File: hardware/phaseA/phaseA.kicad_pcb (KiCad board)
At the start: 2 copper layers, 160 x 50 mm, 39 parts, among them K1 AQY212GH, U1 TXS0108EPWR, U2 TXS0108EPWR, U3 TXS0108EPWR, U4 TXS0108EPWR, U5 TXS0108EPWR, U6 TXS0108EPWR, U7 LM393

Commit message: Phase A: import SES scripté (parseur s-expression, l'import natif KiCad échoue), R8 hystérésis ajoutée au PCB, rendu visuel OK, passe 2 de routage en cours (freerouting 2.2.4/JDK25, bug -mp contourné)
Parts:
- added R8: 1M, R_0603_1608Metric, F.Cu at (55.5, 13.2)
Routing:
- net +3V3: track 0.00 -> 295.9 mm, vias 0 -> 14
- net +5V: track 0.00 -> 251.5 mm, vias 0 -> 12
- net OE_EN: track 0.00 -> 160.0 mm, vias 0 -> 4
- net D1: track 0.00 -> 143.4 mm, vias 0 -> 3
- net A2: track 0.00 -> 135.7 mm, vias 0 -> 2
- net D4: track 0.00 -> 133.8 mm, vias 0 -> 1
- net A3: track 0.00 -> 128.8 mm, vias 0 -> 2
- net A4: track 0.00 -> 126.6 mm, vias 0 -> 3
- net A0: track 0.00 -> 125.6 mm, vias 0 -> 1
- net D0: track 0.00 -> 124.2 mm, vias 0 -> 3
- net PHI2: track 0.00 -> 118.6 mm, vias 0 -> 1
- net D2: track 0.00 -> 118.5 mm, vias 0 -> 1
- net IO_n: track 0.00 -> 116.7 mm, vias 0 -> 1
- net A6: track 0.00 -> 116.0 mm, vias 0 -> 1
- net A10: track 0.00 -> 116.0 mm, vias 0 -> 1
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
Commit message: Phase A: pinout J_ULX_A réordonné (fan-out monotone vers les TXS), règles fines 0,2/0,15, routeur A* d'appoint, netclass alignée — routage r8 en cours
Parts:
- moved R8 8.55 mm to (59.0, 21.0), turned to 90 degrees
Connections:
- J_ULX_A pad 1: A0 -> RW
- J_ULX_A pad 10: A9 -> D0
- J_ULX_A pad 11: A10 -> D1
- J_ULX_A pad 12: A11 -> D2
- J_ULX_A pad 13: A12 -> D3
- J_ULX_A pad 14: A13 -> D4
- J_ULX_A pad 15: A14 -> D5
- J_ULX_A pad 16: A15 -> D6
- J_ULX_A pad 17: D0 -> D7
- J_ULX_A pad 18: D1 -> A0
- J_ULX_A pad 19: D2 -> A1
- J_ULX_A pad 2: A1 -> PHI2
- J_ULX_A pad 20: D3 -> A2
- J_ULX_A pad 21: D4 -> A3
- J_ULX_A pad 22: D5 -> A4
- J_ULX_A pad 23: D6 -> A5
- J_ULX_A pad 24: D7 -> A6
- J_ULX_A pad 25: RW -> A7
- J_ULX_A pad 26: PHI2 -> A8
- J_ULX_A pad 27: IO_n -> A9
- J_ULX_A pad 28: RST_n -> A10
- J_ULX_A pad 29: IRQ_n -> A11
- J_ULX_A pad 3: A2 -> IO_n
- J_ULX_A pad 30: ROMDIS_n -> A12
- J_ULX_A pad 31: MAP_n -> A13
- J_ULX_A pad 32: IOCTL_n -> A14
- J_ULX_A pad 33: OE_EN -> A15
- J_ULX_A pad 4: A3 -> RST_n
- J_ULX_A pad 5: A4 -> IRQ_n
- J_ULX_A pad 6: A5 -> ROMDIS_n
- J_ULX_A pad 7: A6 -> MAP_n
- J_ULX_A pad 8: A7 -> IOCTL_n
- J_ULX_A pad 9: A8 -> OE_EN
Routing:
- net +3V3: track 295.9 -> 0.00 mm, vias 14 -> 0
- net +5V: track 251.5 -> 0.00 mm, vias 12 -> 0
- net OE_EN: track 160.0 -> 0.00 mm, vias 4 -> 0
- net D1: track 143.4 -> 0.00 mm, vias 3 -> 0
- net A2: track 135.7 -> 0.00 mm, vias 2 -> 0
- net D4: track 133.8 -> 0.00 mm, vias 1 -> 0
- net A3: track 128.8 -> 0.00 mm, vias 2 -> 0
- net A4: track 126.6 -> 0.00 mm, vias 3 -> 0
- net A0: track 125.6 -> 0.00 mm, vias 1 -> 0
- net D0: track 124.2 -> 0.00 mm, vias 3 -> 0
- net PHI2: track 118.6 -> 0.00 mm, vias 1 -> 0
- net D2: track 118.5 -> 0.00 mm, vias 1 -> 0
- net IO_n: track 116.7 -> 0.00 mm, vias 1 -> 0
- net A6: track 116.0 -> 0.00 mm, vias 1 -> 0
- net A10: track 116.0 -> 0.00 mm, vias 1 -> 0
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
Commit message: Phase A: carte agrandie 160x56 (autoroute sud pour le fan-out header), outillage complet de routage (A* nom-de-net, import SES, boucle de re-routage), diagnostics (bug freerouting: omission silencieuse aléatoire de nets, crash sur ':' dans les noms d'images DSN)
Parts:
- removed the J_CAS at (0.00, 0.00)
- removed the J_EXP at (0.00, 0.00)
- added J_CAS: DIN41524_7pin_270deg_Female, DIN41524_7pin_270deg_Female, F.Cu at (0.00, 0.00)
- added J_EXP: EDGE_34_GOLDFINGERS, JEXP_34_GOLDFINGERS, F.Cu at (0.00, 0.00)
- moved J_ULX_A 6.00 mm to (14.0, 52.5)
- moved J_ULX_B 6.00 mm to (72.0, 52.5)
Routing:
- net +3V3: track 0.00 -> 271.1 mm, vias 0 -> 8
- net +5V: track 0.00 -> 239.1 mm, vias 0 -> 5
- net OE_EN: track 0.00 -> 174.5 mm, vias 0 -> 5
- net RW: track 0.00 -> 162.1 mm, vias 0 -> 1
- net PHI2: track 0.00 -> 150.3 mm, vias 0 -> 3
- net RST_n: track 0.00 -> 147.1 mm, vias 0 -> 3
- net MAP_n: track 0.00 -> 143.4 mm, vias 0 -> 2
- net IO_n: track 0.00 -> 143.1 mm, vias 0 -> 3
- net IRQ_n: track 0.00 -> 141.4 mm, vias 0 -> 2
- net IOCTL_n: track 0.00 -> 138.0 mm, vias 0 -> 2
- net ROMDIS_n: track 0.00 -> 137.8 mm, vias 0 -> 2
- net D0: track 0.00 -> 129.1 mm, vias 0 -> 2
- net D1: track 0.00 -> 127.7 mm, vias 0 -> 1
- net D3: track 0.00 -> 125.9 mm, vias 0 -> 3
- net D5: track 0.00 -> 123.5 mm, vias 0 -> 2
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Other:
- board size 160 x 50 mm -> 160 x 56 mm

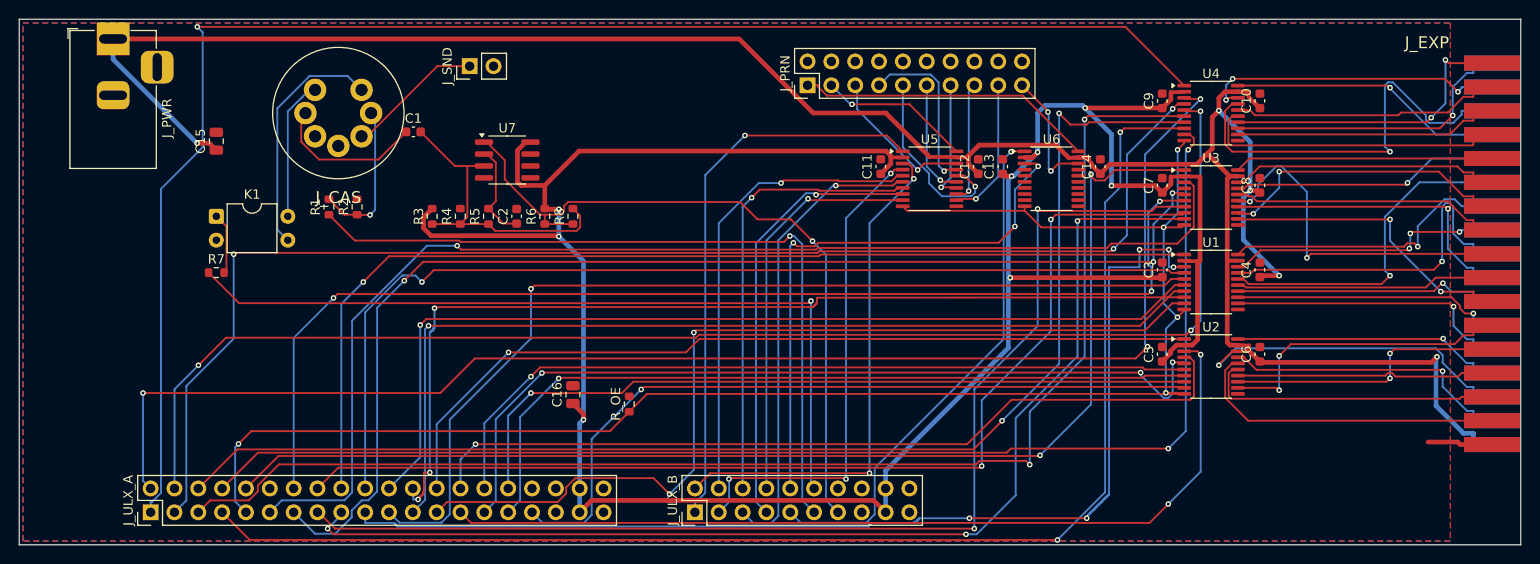
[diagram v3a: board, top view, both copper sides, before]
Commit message: Phase A: PCB routé (144/144 signaux dont 2 tronçons à finir au push-and-shove), 0 erreur DRC, exports fab complets
- Routage final: freerouting 1.9 (DISPLAY local) + A* maison (relais + queues
  validées) + 61 vias de couture GND + suppression d'îlots
- Bugs routeurs documentés et contournés: 2.2.4 omission silencieuse de nets
  (paires de doigts coïncidentes), crash sur ':' dans les noms d'images DSN,
  1.9 headless impossible (HeadlessException)
- Exports: gerbers+perçage, BOM.csv (16 refs), CPL.csv (32 CMS), rendus PNG
- Reste: tronçon central RST5_n et IRQ5_n (queues posées), artefact de
  comptage GND à inspecter en GUI
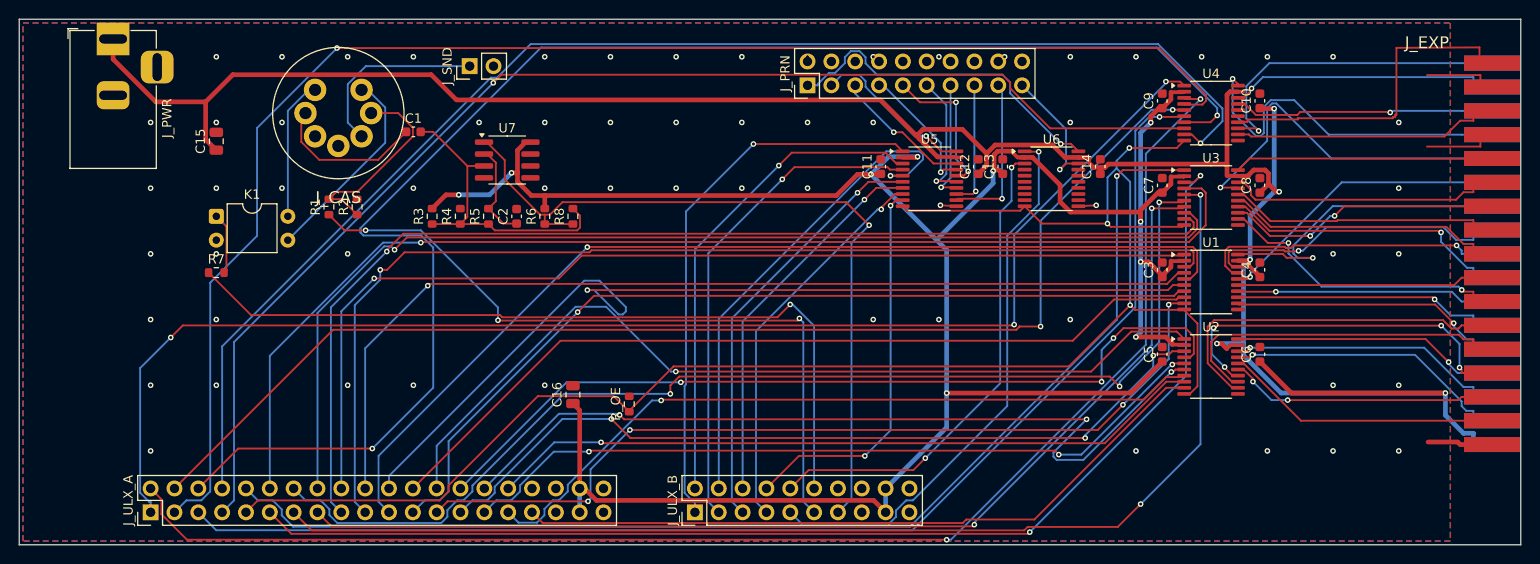
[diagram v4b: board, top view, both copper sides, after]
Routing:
- net D2: track 0.00 -> 125.6 mm, vias 0 -> 1
- net IRQ5_n: track 30.9 -> 8.22 mm
- net ROMDIS_n: track 137.8 -> 159.9 mm
- net RST5_n: track 27.2 -> 8.22 mm
- net IO5_n: track 42.8 -> 25.8 mm
- net RW: track 162.1 -> 145.7 mm, vias 1 -> 3
- net RST_n: track 147.1 -> 130.9 mm, vias 3 -> 2
- net A6: track 104.8 -> 90.6 mm, vias 3 -> 0
- net +5V: track 239.1 -> 253.0 mm
- net +3V3: track 271.1 -> 258.2 mm, vias 8 -> 10
- net A5V13: track 25.5 -> 38.2 mm, vias 0 -> 4
- net IO_n: track 143.1 -> 155.4 mm, vias 3 -> 1
- net D5V2: track 26.4 -> 37.0 mm
- net MAP_n: track 143.4 -> 134.4 mm, vias 2 -> 1
- net OE_EN: track 174.5 -> 183.4 mm, vias 5 -> 3
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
